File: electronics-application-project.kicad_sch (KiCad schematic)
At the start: 42 parts, among them J1 Conn_02x03_Odd_Even, U1 W5500, U2 ARJM11C7-114-BA-EW2, U3 LM2574-3.3YN, U4 ATTINY85-20SU, Y2 ABLS7M2-25.000MHZ-D-2Y-T

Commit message: v2
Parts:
- removed L1: 330uH, Inductor_SMD:L_Wuerth_WE-PD4-Typ-X, symbol Device:L
- added L1: 12LRS334C, Imported:IND_MURATA_1200LRS_MUR, symbol Imported:12LRS334C
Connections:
- net 3.3V_D: now also L1.3 (1)
- net GND: now also U2.1 (VC2-), U3.2 (SIGGND), U3.3 (ON/OFF), U3.4 (PWRGND)
- net at D1.1 (K), U3.7 (OUTPUT): now also L1.1
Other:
- moved on the sheet: D1

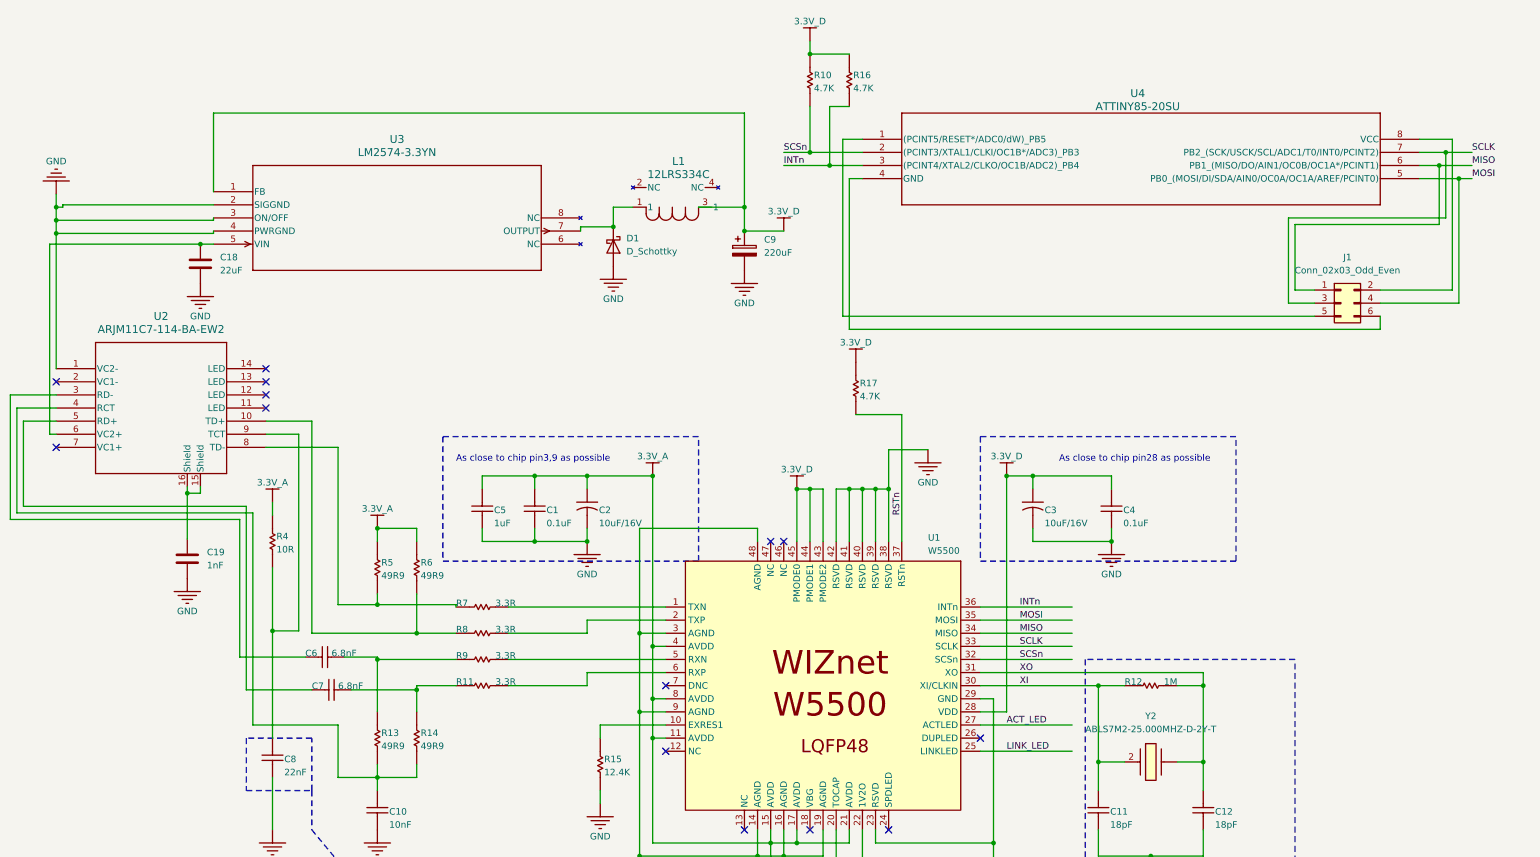
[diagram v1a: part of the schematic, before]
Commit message: add ethernet leds; change power supply capacitors; change attiny85 pin connections;
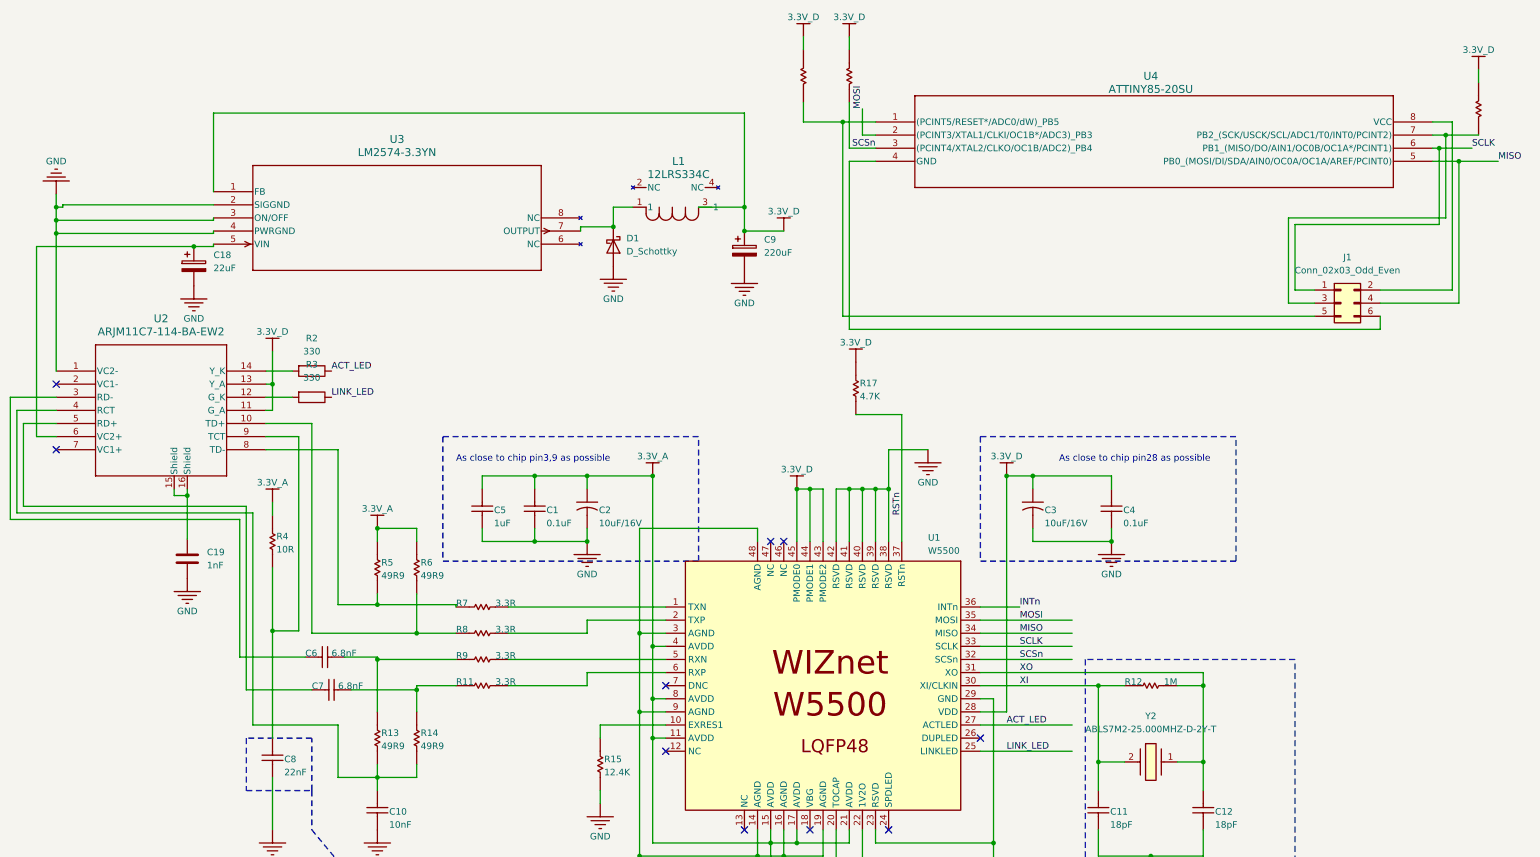
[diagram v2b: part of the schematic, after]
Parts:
- removed C18: 22uF, Capacitor_SMD:C_0805_2012Metric_Pad1.18x1.45mm_HandSolder, symbol Device:C
- added C18: 22uF, Capacitor_SMD:CP_Elec_6.3x5.4, symbol Device:C_Polarized
- added R1: 4.7K, Resistor_SMD:R_0805_2012Metric_Pad1.20x1.40mm_HandSolder, symbol electronics-application-project-altium-import:root_1_RES-0402
- added R2, R3: 330, Resistor_SMD:R_0805_2012Metric_Pad1.20x1.40mm_HandSolder, symbol Device:R
- C19: footprint Capacitor_SMD:C_0805_2012Metric_Pad1.18x1.45mm_HandSolder -> Capacitor_SMD:C_1210_3225Metric_Pad1.33x2.70mm_HandSolder
- C9: footprint Capacitor_THT:CP_Radial_D8.0mm_P3.50mm -> Capacitor_SMD:CP_Elec_8x6.2
- U2: footprint Imported:ARJM11C7-114-BA-EW2_ABR -> Imported:ARJM11C7-114-BA-EW2_ABR-fixed
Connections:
- net 3.3V_D: now also U2.11 (G_A), U2.13 (Y_A), R1.2
- net ACT_LED: now also R2.1
- net GND: now also C18.2
- net INTn: no longer R16.1, U4.3 ((PCINT4/XTAL2/CLKO/OC1B/ADC2)_PB4)
- net LINK_LED: now also R3.1
- net MISO: now also J1.4 (Pin_4), U4.5 (PB0_(MOSI/DI/SDA/AIN0/OC0A/OC1A/AREF/PCINT0)); no longer J1.1 (Pin_1), U4.6 (PB1_(MISO/DO/AIN1/OC0B/OC1A*/PCINT1))
- net MOSI: now also U4.2 ((PCINT3/XTAL1/CLKI/OC1B*/ADC3)_PB3); no longer J1.4 (Pin_4), U4.5 (PB0_(MOSI/DI/SDA/AIN0/OC0A/OC1A/AREF/PCINT0))
- net SCLK: now also J1.1 (Pin_1), U4.6 (PB1_(MISO/DO/AIN1/OC0B/OC1A*/PCINT1)); no longer J1.3 (Pin_3), U4.7 (PB2_(SCK/USCK/SCL/ADC1/T0/INT0/PCINT2))
- net SCSn: now also U4.3 ((PCINT4/XTAL2/CLKO/OC1B/ADC2)_PB4); no longer U4.2 ((PCINT3/XTAL1/CLKI/OC1B*/ADC3)_PB3)
- net XO: now also Y2.1; no longer Y2.
- net at J1.5 (Pin_5), U4.1 ((PCINT5/RESET*/ADC0/dW)_PB5): now also R16.1
- net at U2.6 (VC2+), U3.5 (VIN): now also C18.1
- net at U2.12 (G_K): now also R3.2
- net at U2.14 (Y_K): now also R2.2
- new net: J1.3 (Pin_3), R1.1, U4.7 (PB2_(SCK/USCK/SCL/ADC1/T0/INT0/PCINT2))
- no-connect marks 14 -> 10
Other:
- moved on the sheet: U4

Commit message: start over
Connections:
- net INTn: now also J1.3 (Pin_3), R1.1, U4.7 (PB2_(SCK/USCK/SCL/ADC1/T0/INT0/PCINT2))
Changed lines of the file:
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@@
+	)
+	(junction
+		(at 285.75 26.67)
+		(diameter 0)
+		(color 0 0 0 0)
 	)
 	(junction
@@
 	(wire
 		(pts
+			(xy 290.83 26.67) (xy 290.83 20.32)
+		)
+		(stroke
+			(width 0)
+			(type default)
+		)
+	)
+	(wire
+		(pts
 			(xy 281.94 31.75) (xy 276.86 31.75)
 		)
@@
 		(pts
 			(xy 212.09 133.35) (xy 212.09 148.1328)
+		)
+		(stroke
+			(width 0)
+			(type default)
+		)
+	)
+	(wire
+		(pts
+			(xy 285.75 26.67) (xy 290.83 26.67)
 		)
 		(stroke
@@
 		(effects
 			(font
+				(size 1.27 1.27)
+			)
+			(justify left bottom)
+		)
+	)
+	(label "INTn"
+		(at 290.83 20.32 0)
+		(effects
+			(font

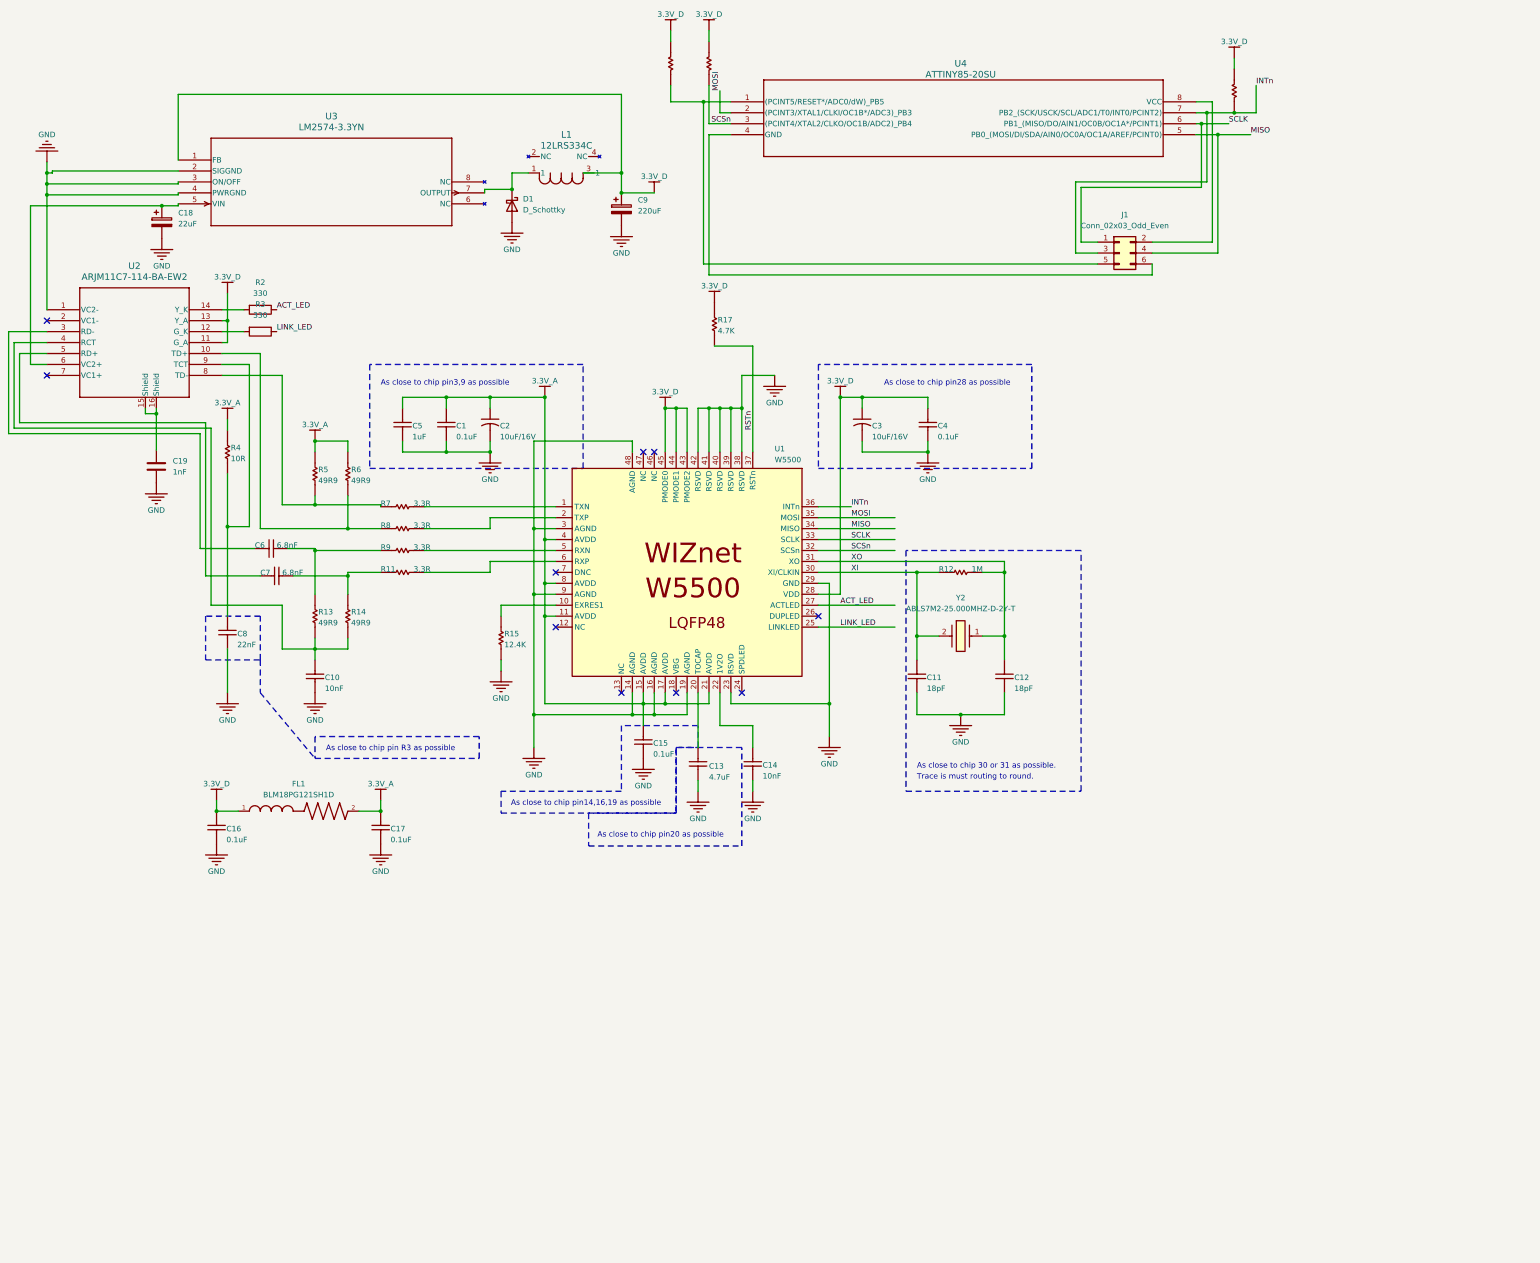
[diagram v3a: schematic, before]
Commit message: add NAND gates and a pin header for UART and PWM; add buzzer; add pin header for GND and 3.3V_D; expand ATtiny85 pin header to all pins; join W5500 RST and ATtiny85 RST and add a pin header for the net;
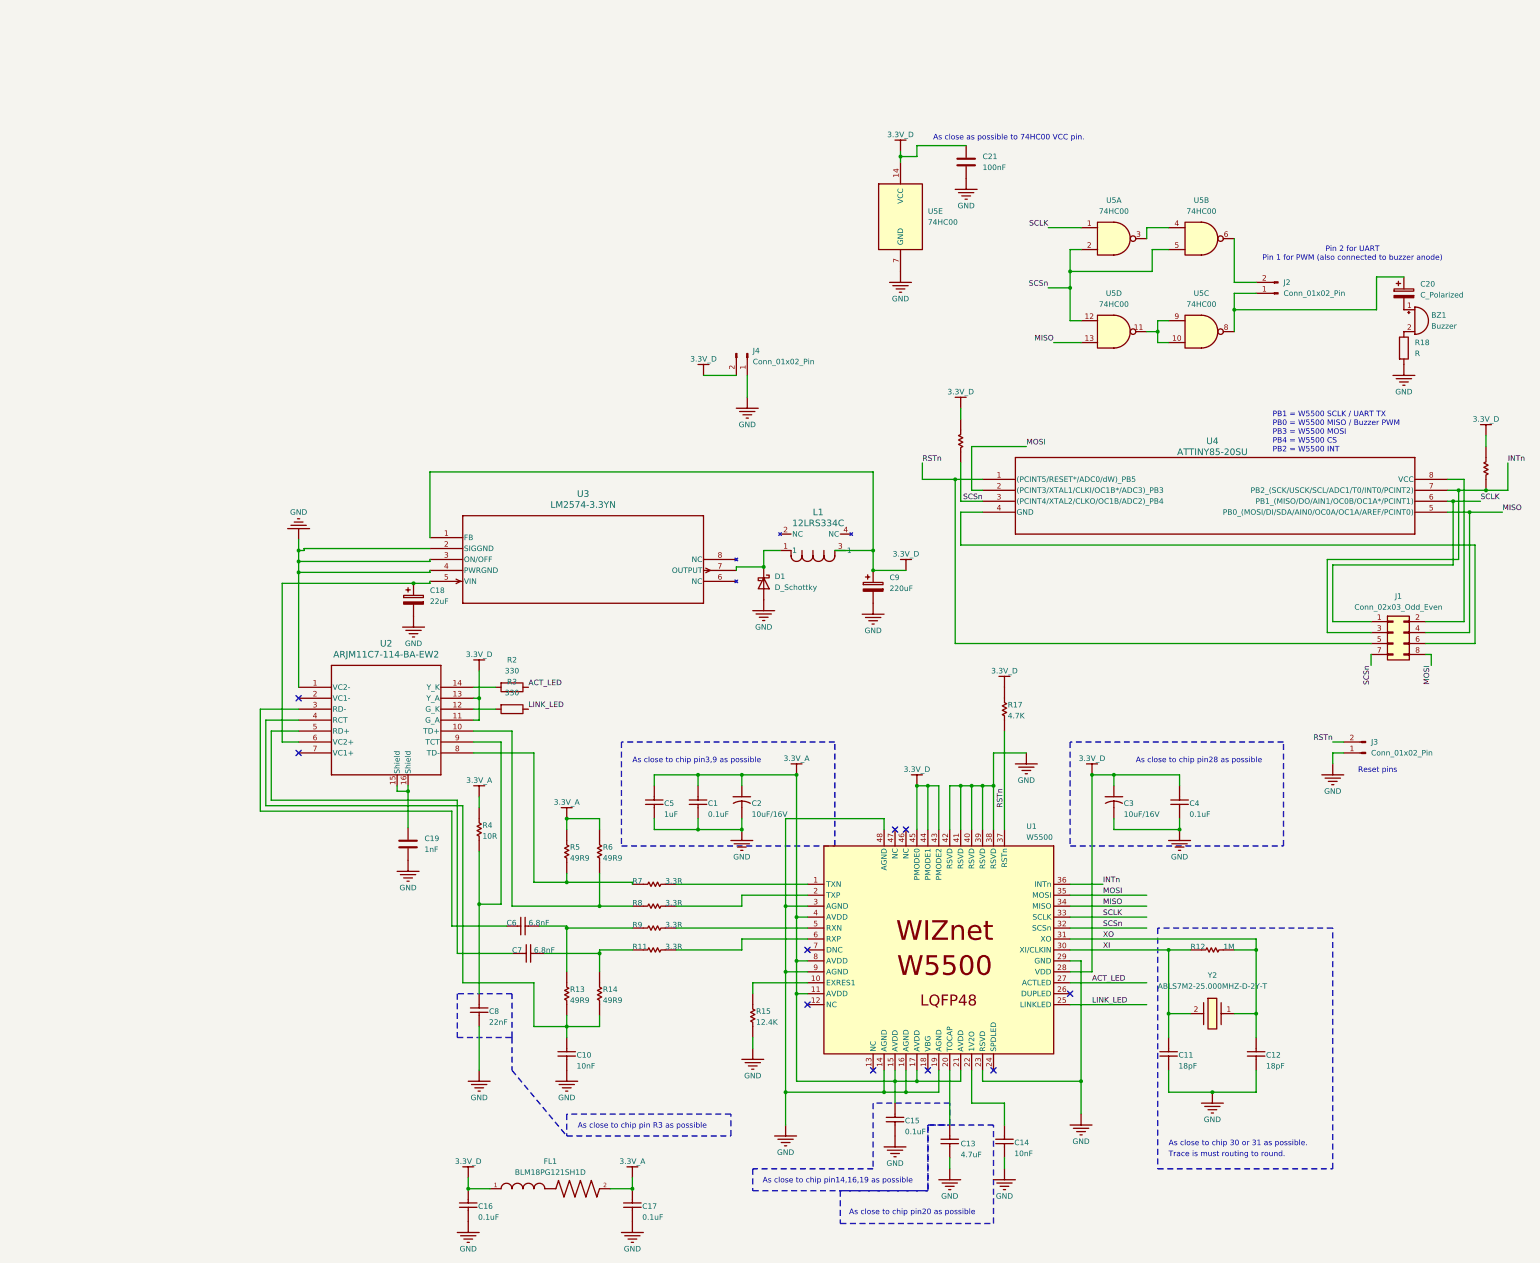
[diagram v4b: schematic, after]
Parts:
- removed R16: 4.7K, Resistor_SMD:R_0805_2012Metric_Pad1.20x1.40mm_HandSolder, symbol electronics-application-project-altium-import:root_1_RES-0402
- added BZ1: Buzzer, Buzzer_Beeper:Buzzer_12x9.5RM7.6, symbol Device:Buzzer
- added C20: C_Polarized, Capacitor_SMD:C_0805_2012Metric_Pad1.18x1.45mm_HandSolder, symbol Device:C_Polarized
- added C21: 100nF, Capacitor_SMD:C_0805_2012Metric_Pad1.18x1.45mm_HandSolder, symbol Device:C
- added J2, J3, J4: Conn_01x02_Pin, Connector_PinHeader_2.54mm:PinHeader_1x02_P2.54mm_Vertical, symbol Connector:Conn_01x02_Pin
- added R18: R, Resistor_SMD:R_0805_2012Metric_Pad1.20x1.40mm_HandSolder, symbol Device:R
- added U5: 74HC00, Package_SO:SO-14_3.9x8.65mm_P1.27mm, symbol 74xx:74HC00
- J1: footprint Connector_PinHeader_2.54mm:PinHeader_2x03_P2.54mm_Vertical -> Connector_PinHeader_2.54mm:PinHeader_2x04_P2.54mm_Vertical; symbol Connector_Generic:Conn_02x03_Odd_Even -> Connector_Generic:Conn_02x04_Odd_Even
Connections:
- net 3.3V_D: now also C21.1, J4.2 (Pin_2), U5.14 (VCC)
- net GND: now also C21.2, J3.1 (Pin_1), J4.1 (Pin_1), R18.2, U5.7 (GND)
- net MISO: now also U5.13
- net MOSI: now also J1.8 (Pin_8)
- net RSTn: now also J1.5 (Pin_5), U4.1 ((PCINT5/RESET*/ADC0/dW)_PB5), J3.2 (Pin_2)
- net SCLK: now also U5.1
- net SCSn: now also J1.7 (Pin_7), U5.12, U5.2, U5.5
- new net: U5.3, U5.4
- new net: J2.2 (Pin_2), U5.6
- new net: BZ1.1 (+), C20.2
- new net: BZ1.2 (-), R18.1
- new net: U5.10, U5.11, U5.9
- new net: C20.1, J2.1 (Pin_1), U5.8
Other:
- note added: "As close as possible to 74HC00 VCC pin."
- note added: "PB1 = W5500 SCLK / UART TX PB0 = W5500 MISO / Buzzer PWM PB3 = W5500 MOSI PB4 = W5500 CS PB2 = W5500 INT"
- note added: "Pin 2 for UART Pin 1 for PWM (also connected to buzzer anode)"
- note added: "Reset pins"
- moved on the sheet: C1, C10, C11, C12, C13, C14, C15, C16, C17, C18, C19, C2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
